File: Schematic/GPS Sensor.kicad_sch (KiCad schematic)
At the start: 35 parts, among them J13 SMA, J21 USB_C_Receptacle_USB2.0_14P, J22 EXT_GPS, J23 GPS_VCC, J24 GPS_RX, J25 GPS_TX, U23 ZED-F9P-15B

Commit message: 1st Schematic Review
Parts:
- renumbered BT2 to BT1, C206 to C192, C207 to C193, C208 to C194, C209 to C195, C210 to C196, C211 to C197, C212 to C198, C213 to C199, C198 to C200, D51 to D48, D47 to D49, D52 to D50, D54 to D51, D53 to D52, D50 to D53, J21 to J22, J22 to J23, J23 to J24, J24 to J25, J25 to J26, J13 to J27, L5 to L4, R163 to R149, R161 to R150, R164 to R151, R165 to R152, R166 to R153, R167 to R154, R168 to R155, R158 to R156, R159 to R157, R160 to R158, R154 to R159, U23 to U24
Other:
- note added: "MAX current draw is 130mA"
- note added: "Max current draw from NEO-6 is 67mA"

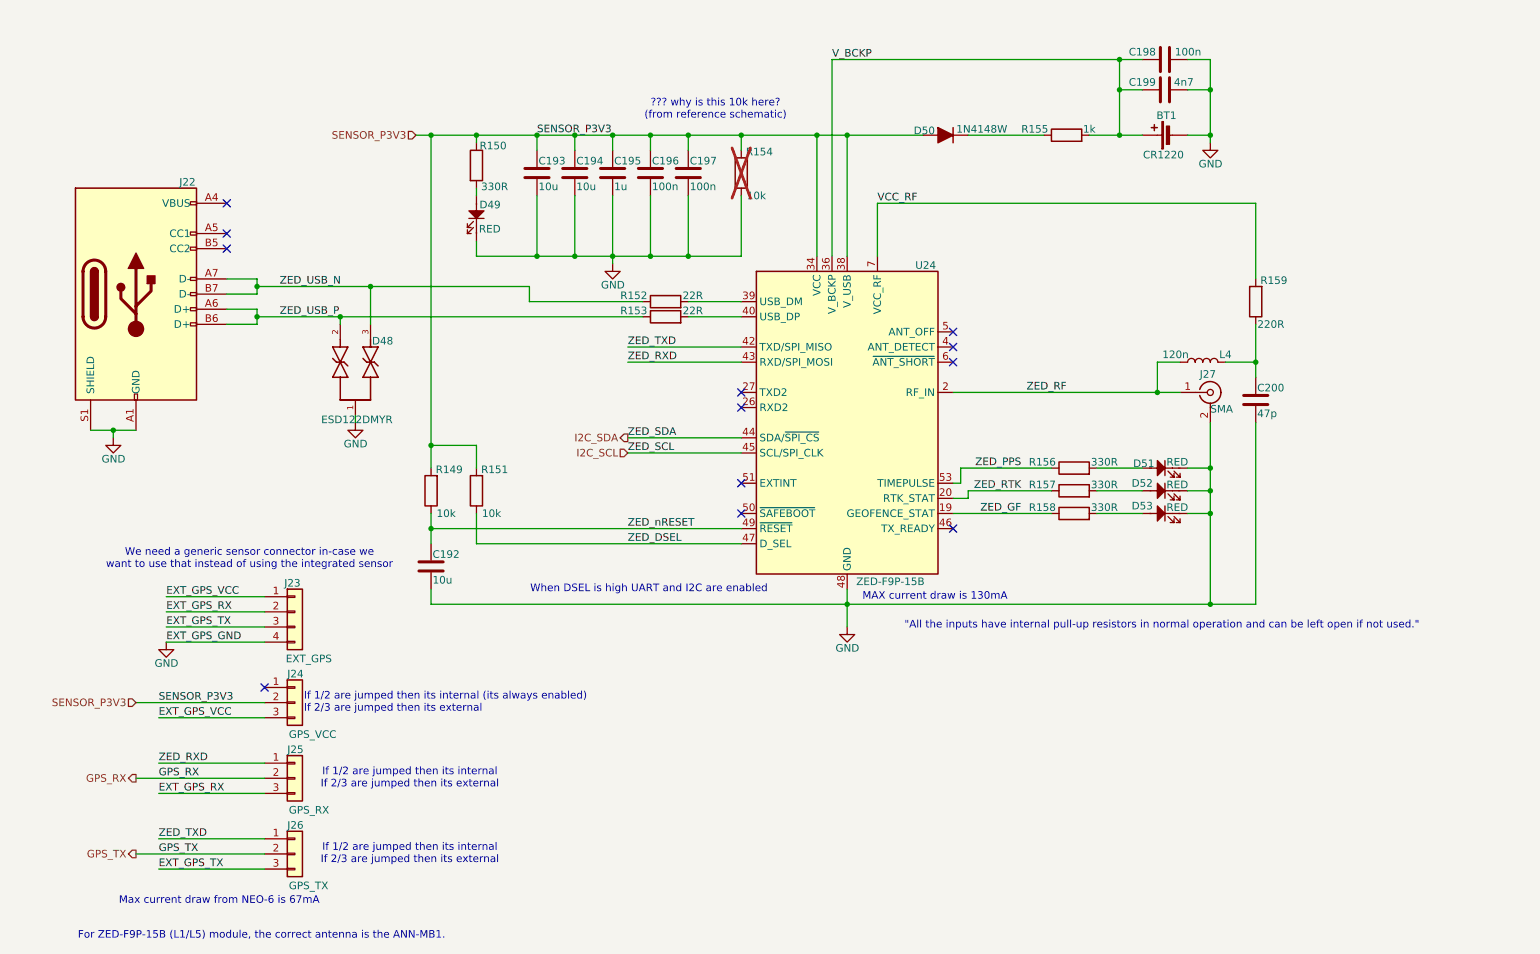
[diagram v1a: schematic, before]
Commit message: added so many test points
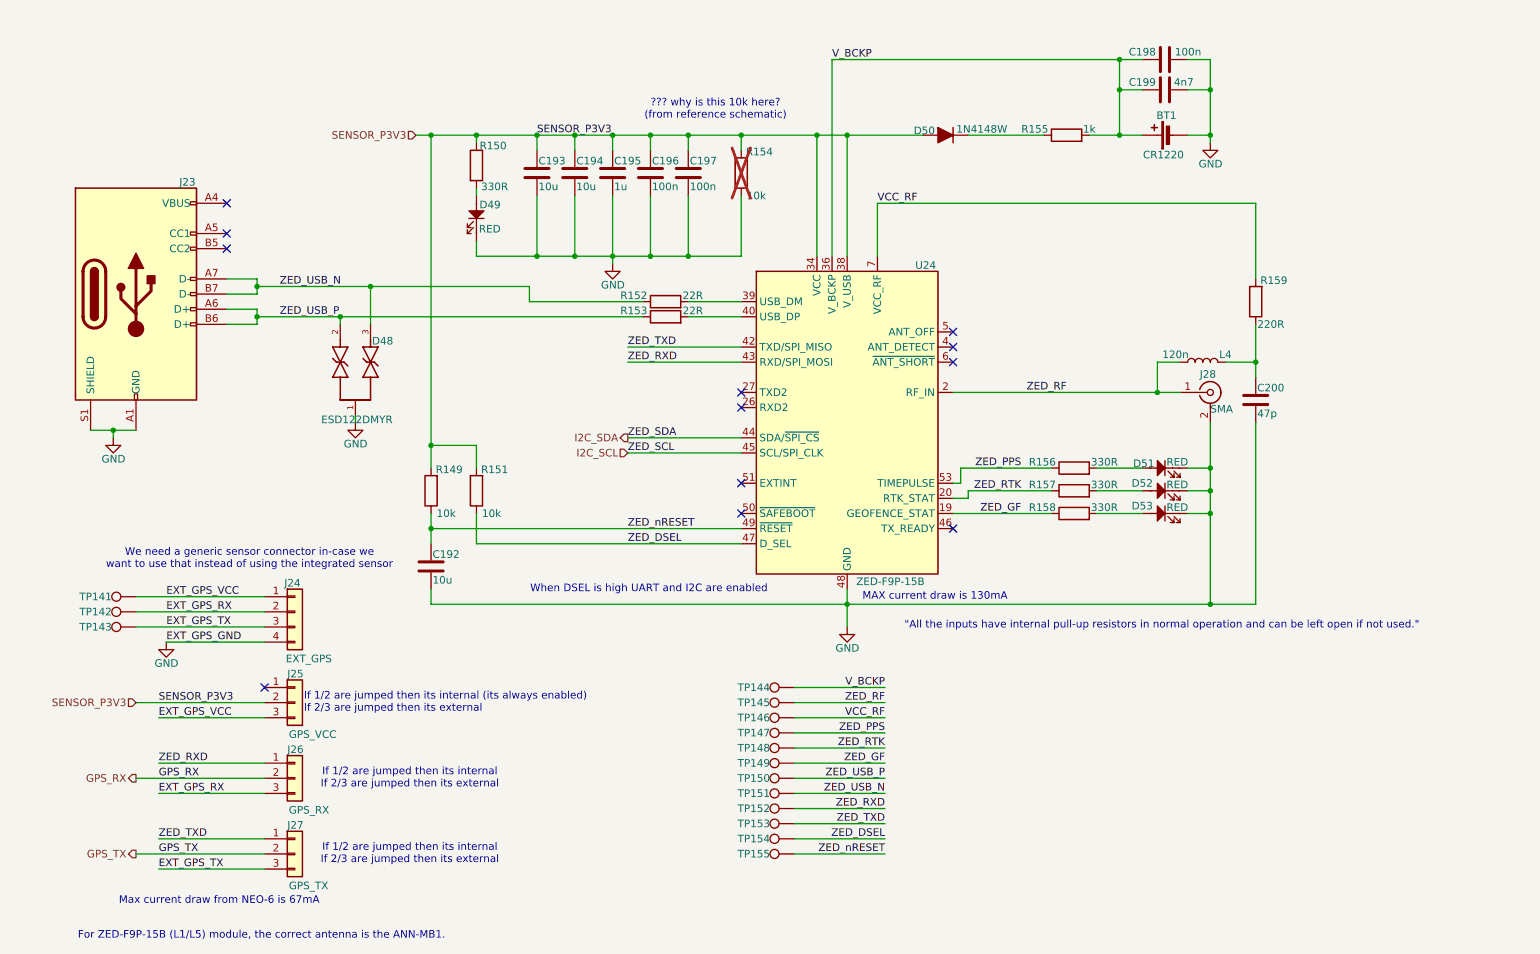
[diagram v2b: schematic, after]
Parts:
- added TP141, TP142, TP143, TP144, TP145, TP146, TP147, TP148, TP149, TP150, TP151, TP152, TP153, TP154, TP155: TestPoint, symbol Connector:TestPoint
- renumbered J22 to J23, J23 to J24, J24 to J25, J25 to J26, J26 to J27, J27 to J28
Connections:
- net EXT_GPS_RX: now also TP142.1
- net EXT_GPS_TX: now also TP143.1
- net EXT_GPS_VCC: now also TP141.1
- net VCC_RF: now also TP146.1
- net V_BCKP: now also TP144.1
- net ZED_DSEL: now also TP154.1
- net ZED_GF: now also TP149.1
- net ZED_PPS: now also TP147.1
- net ZED_RF: now also TP145.1
- net ZED_RTK: now also TP148.1
- net ZED_RXD: now also TP152.1
- net ZED_TXD: now also TP153.1
- net ZED_USB_N: now also TP151.1
- net ZED_USB_P: now also TP150.1
- net ZED_nRESET: now also TP155.1

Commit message: updates
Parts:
- renumbered C192 to C194, C193 to C195, C194 to C196, C195 to C197, C196 to C198, C197 to C199, C198 to C200, C199 to C201, C200 to C202, D48 to D50, D49 to D51, D50 to D52, D51 to D53, D52 to D54, D53 to D55, J23 to J25, J24 to J26, J25 to J27, J26 to J28, J27 to J29, J28 to J30, R149 to R162, R150 to R163, R151 to R164, R152 to R165, R153 to R166, R154 to R167, R155 to R168, R156 to R169, R157 to R170, R158 to R171, R159 to R172

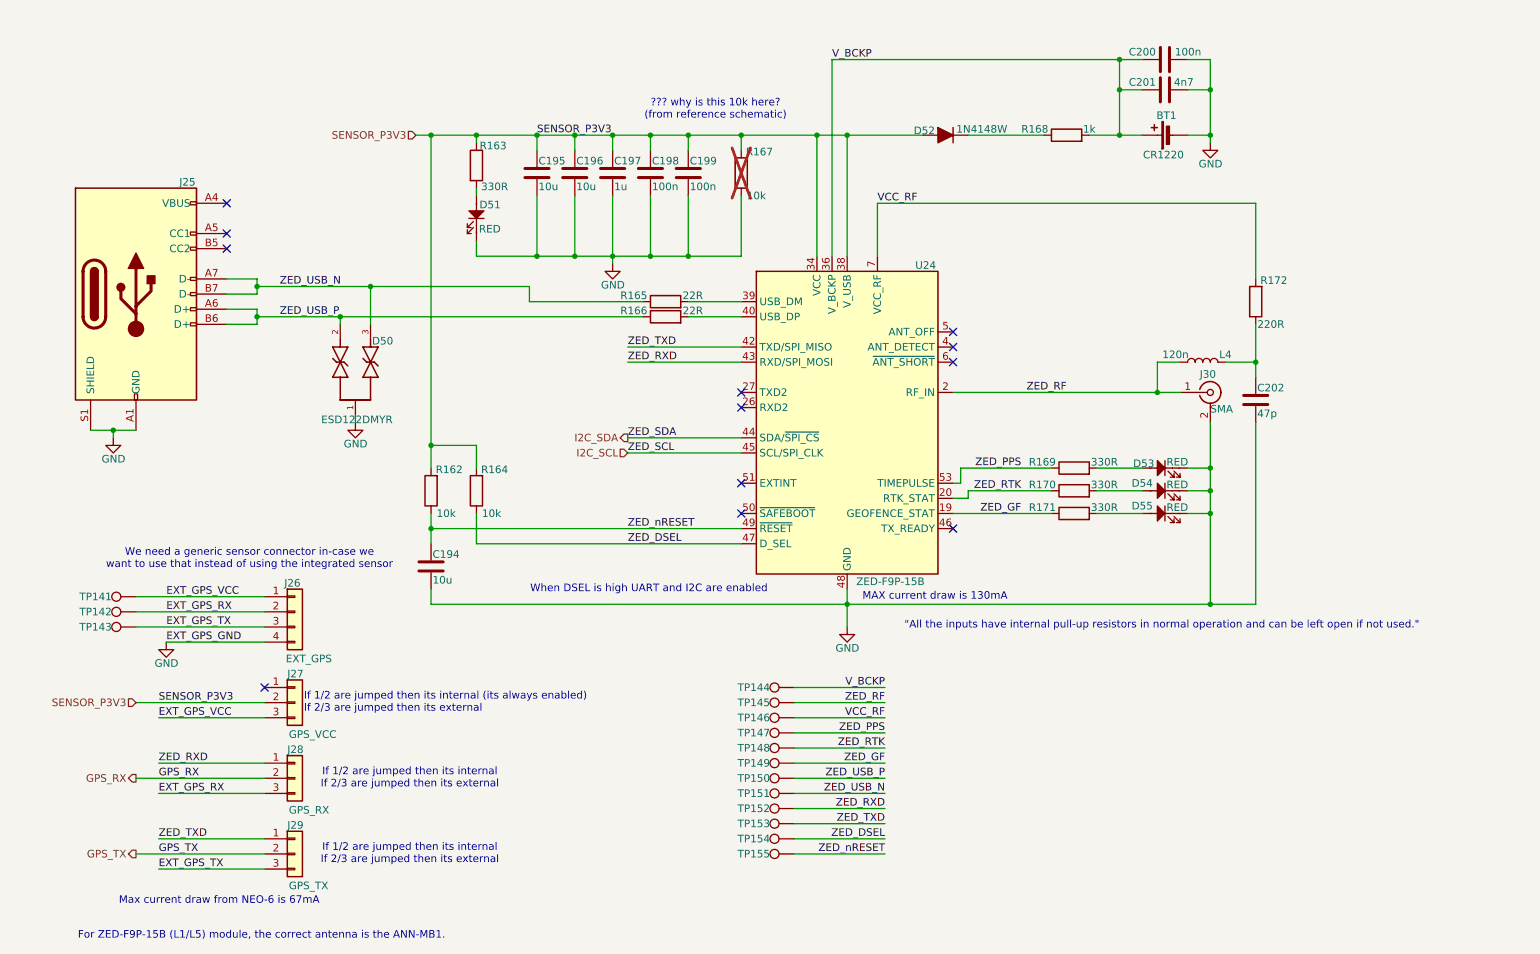
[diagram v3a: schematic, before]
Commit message: updated fuel guage
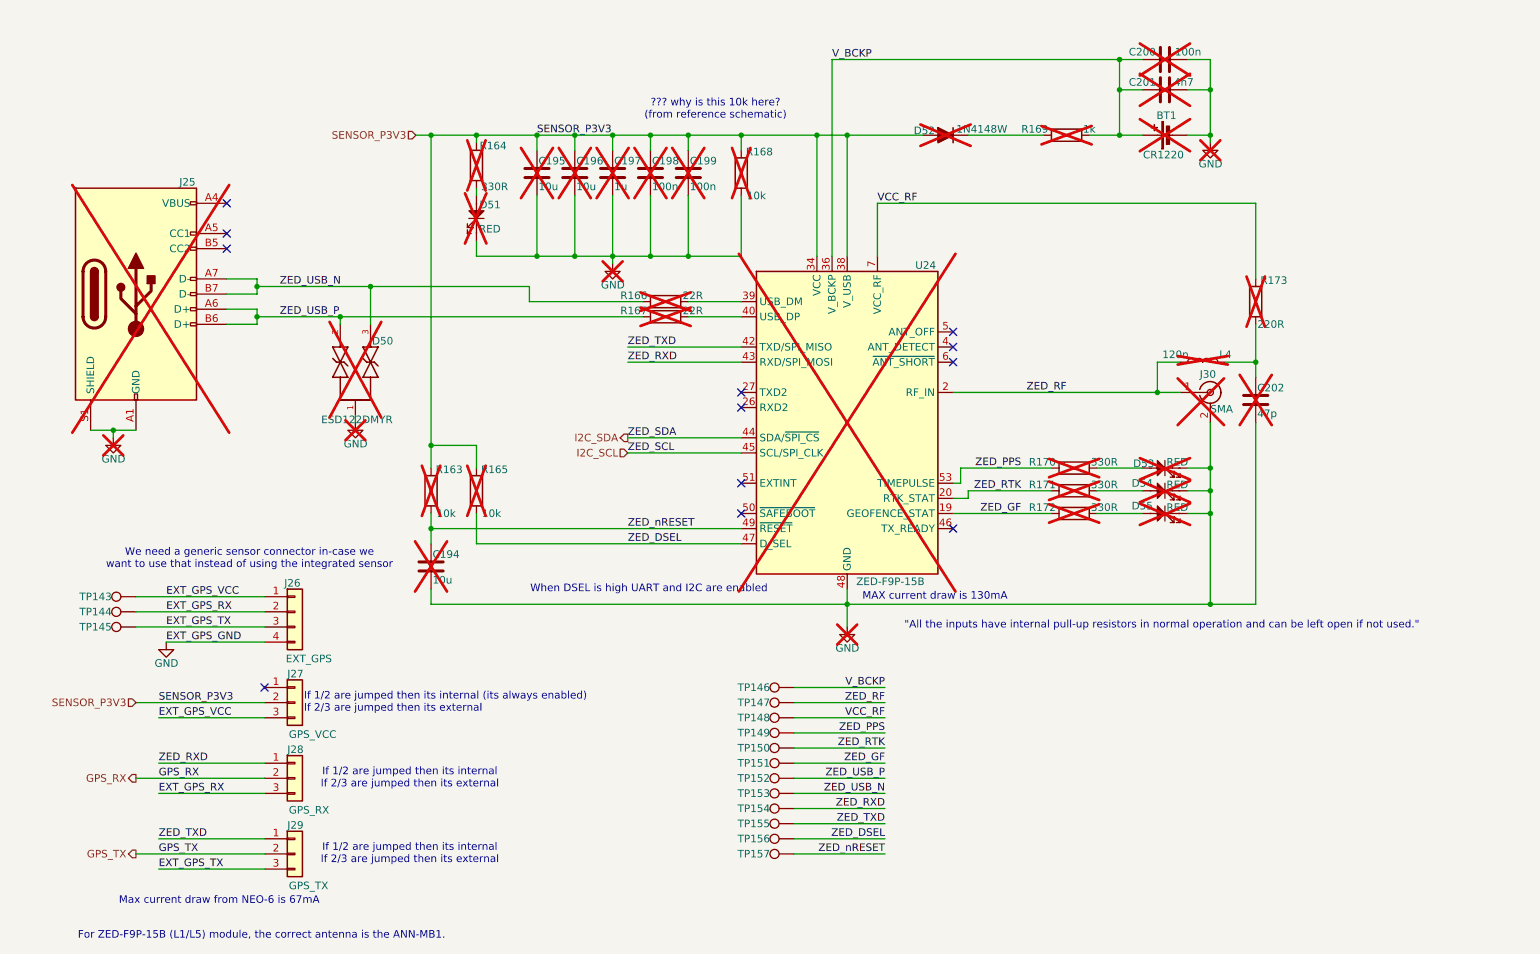
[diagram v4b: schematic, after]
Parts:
- BT1, C194, C195, C196, C197, C198, C199, C200, C201, C202, D50, D51, D52, D53, D54, D55, J25, J30, L4, U24: now not fitted
- R163: renamed from R162; now not fitted
- R164: renamed from R163; now not fitted
- R165: renamed from R164; now not fitted
- R166: renamed from R165; now not fitted
- R167: renamed from R166; now not fitted
- R169: renamed from R168; now not fitted
- R170: renamed from R169; now not fitted
- R171: renamed from R170; now not fitted
- R172: renamed from R171; now not fitted
- R173: renamed from R172; now not fitted
- renumbered R167 to R168, TP141 to TP143, TP142 to TP144, TP143 to TP145, TP144 to TP146, TP145 to TP147, TP146 to TP148, TP147 to TP149, TP148 to TP150, TP149 to TP151, TP150 to TP152, TP151 to TP153, TP152 to TP154, TP153 to TP155, TP154 to TP156, TP155 to TP157

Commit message: Added MCU
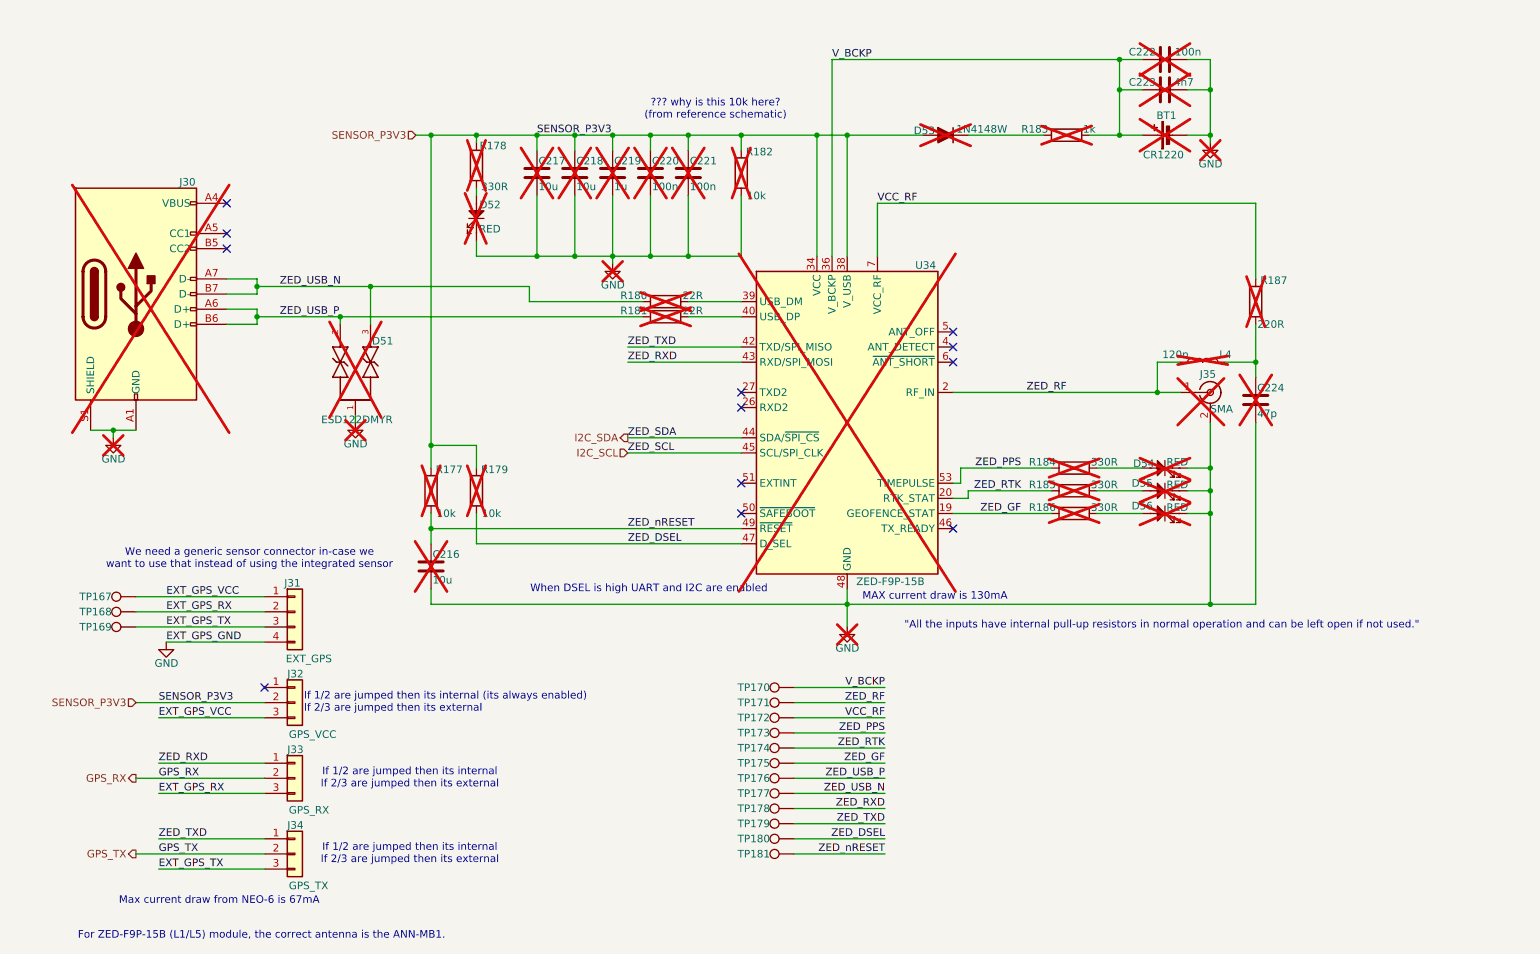
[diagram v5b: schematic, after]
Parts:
- renumbered C194 to C216, C195 to C217, C196 to C218, C197 to C219, C198 to C220, C199 to C221, C200 to C222, C201 to C223, C202 to C224, D50 to D51, D51 to D52, D52 to D53, D53 to D54, D54 to D55, D55 to D56, J25 to J30, J26 to J31, J27 to J32, J28 to J33, J29 to J34, J30 to J35, R163 to R177, R164 to R178, R165 to R179, R166 to R180, R167 to R181, R168 to R182, R169 to R183, R170 to R184, R171 to R185, R172 to R186, R173 to R187, TP143 to TP167, TP144 to TP168, TP145 to TP169, TP146 to TP170, TP147 to TP171, TP148 to TP172, TP149 to TP173, TP150 to TP174, TP151 to TP175, TP152 to TP176, TP153 to TP177, TP154 to TP178, TP155 to TP179, TP156 to TP180, TP157 to TP181, U24 to U34
